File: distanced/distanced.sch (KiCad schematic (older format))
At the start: 20 parts

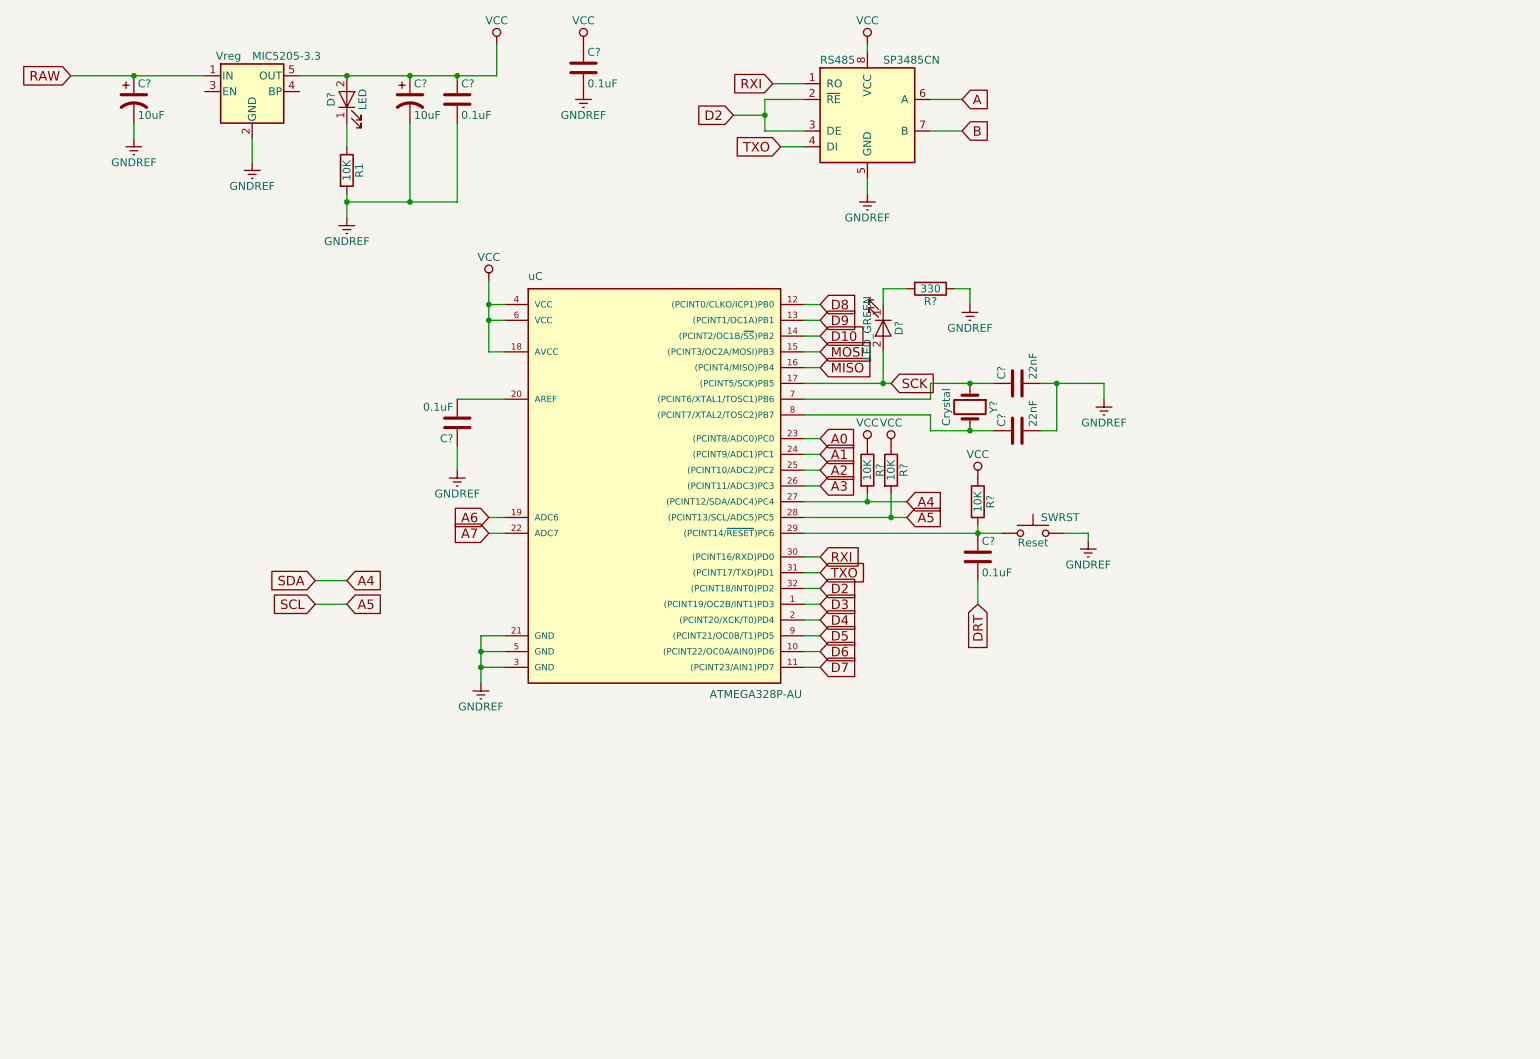
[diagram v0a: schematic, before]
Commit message: added the schematic of the ToF sensor
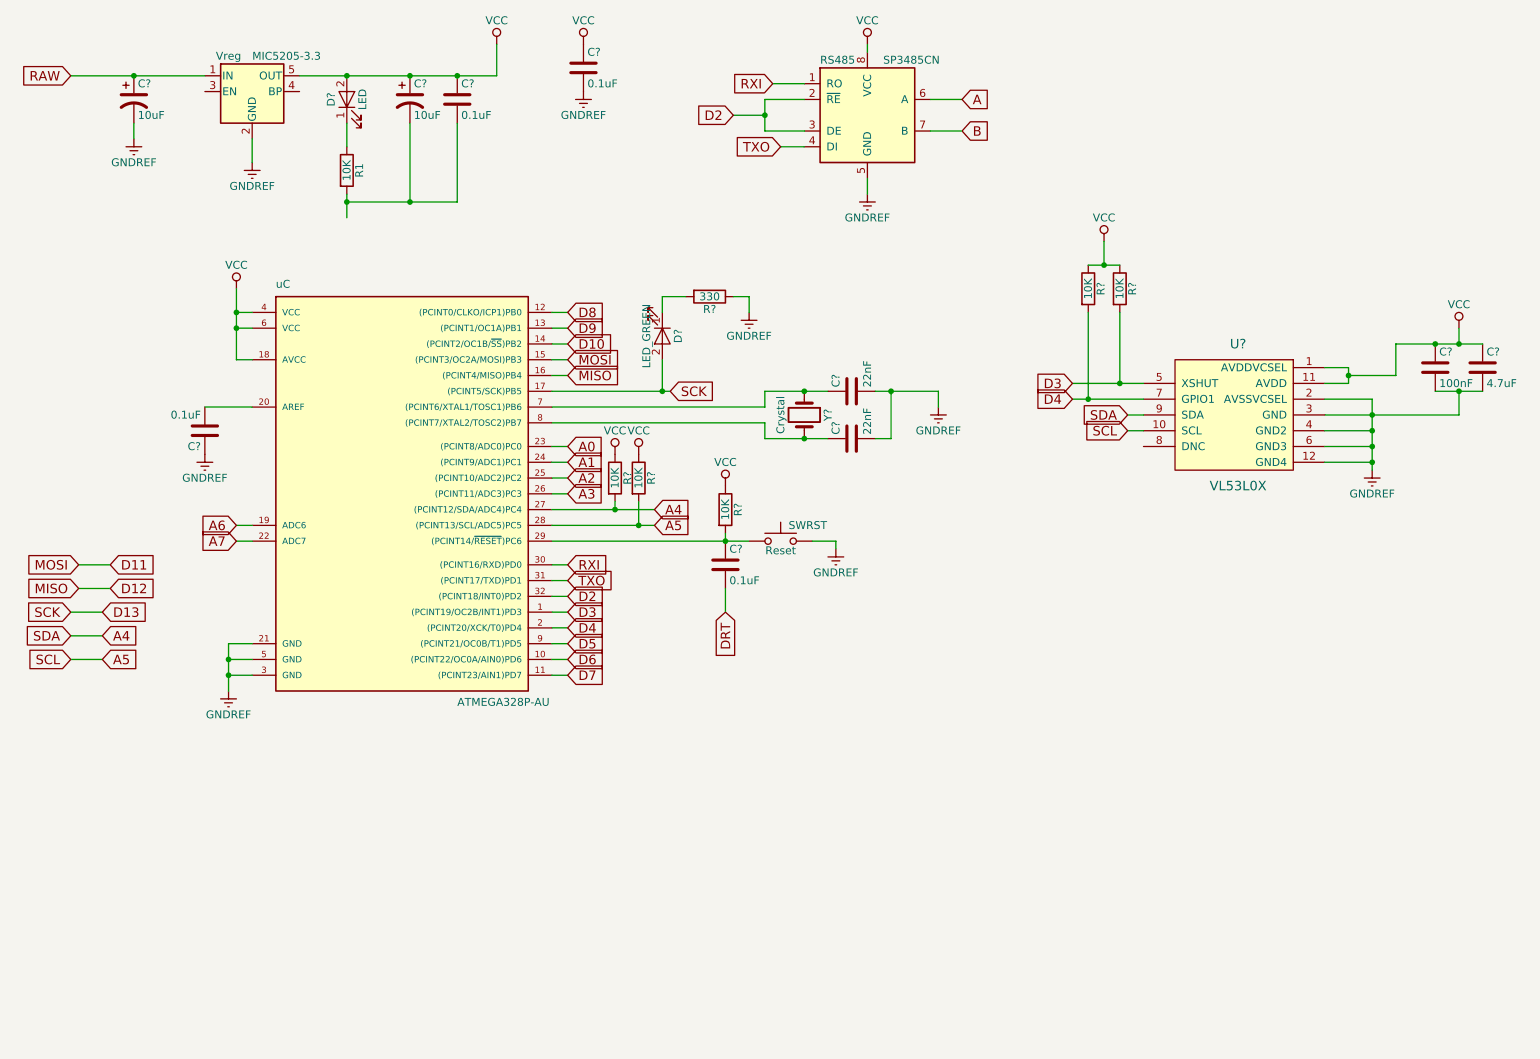
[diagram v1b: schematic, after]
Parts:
- added C?: 100nF, symbol C
- added C?: 4.7uF, symbol C
- added R? (x2): 10K, symbol R
- added U?: VL53L0X, symbol VL53L0X
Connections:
- net A4: now also U?.9 (SDA)
- net A5: now also U?.10 (SCL)
- net D3: now also R?.2, U?.5 (XSHUT)
- net D4: now also R?.2, U?.7 (GPIO1)
- net GNDREF: now also C?.2, C?.2, U?.12 (GND4), U?.2 (AVSSVCSEL), U?.3 (GND), U?.4 (GND2), U?.6 (GND3); no longer C?.2, C?.2, R1.2
- net VCC: now also C?.1, C?.1, R?.1, R?.1, U?.1 (AVDDVCSEL), U?.11 (AVDD)
- net MISO renamed D12
- net MOSI renamed D11
- net SCK renamed D13
- new net: C?.2, C?.2, R1.2
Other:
- moved on the sheet: C?, D?, R?, SWRST, Y?, uC

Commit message: added 2.8Vreg for tof and the ICSP FTDI and RS485 headers
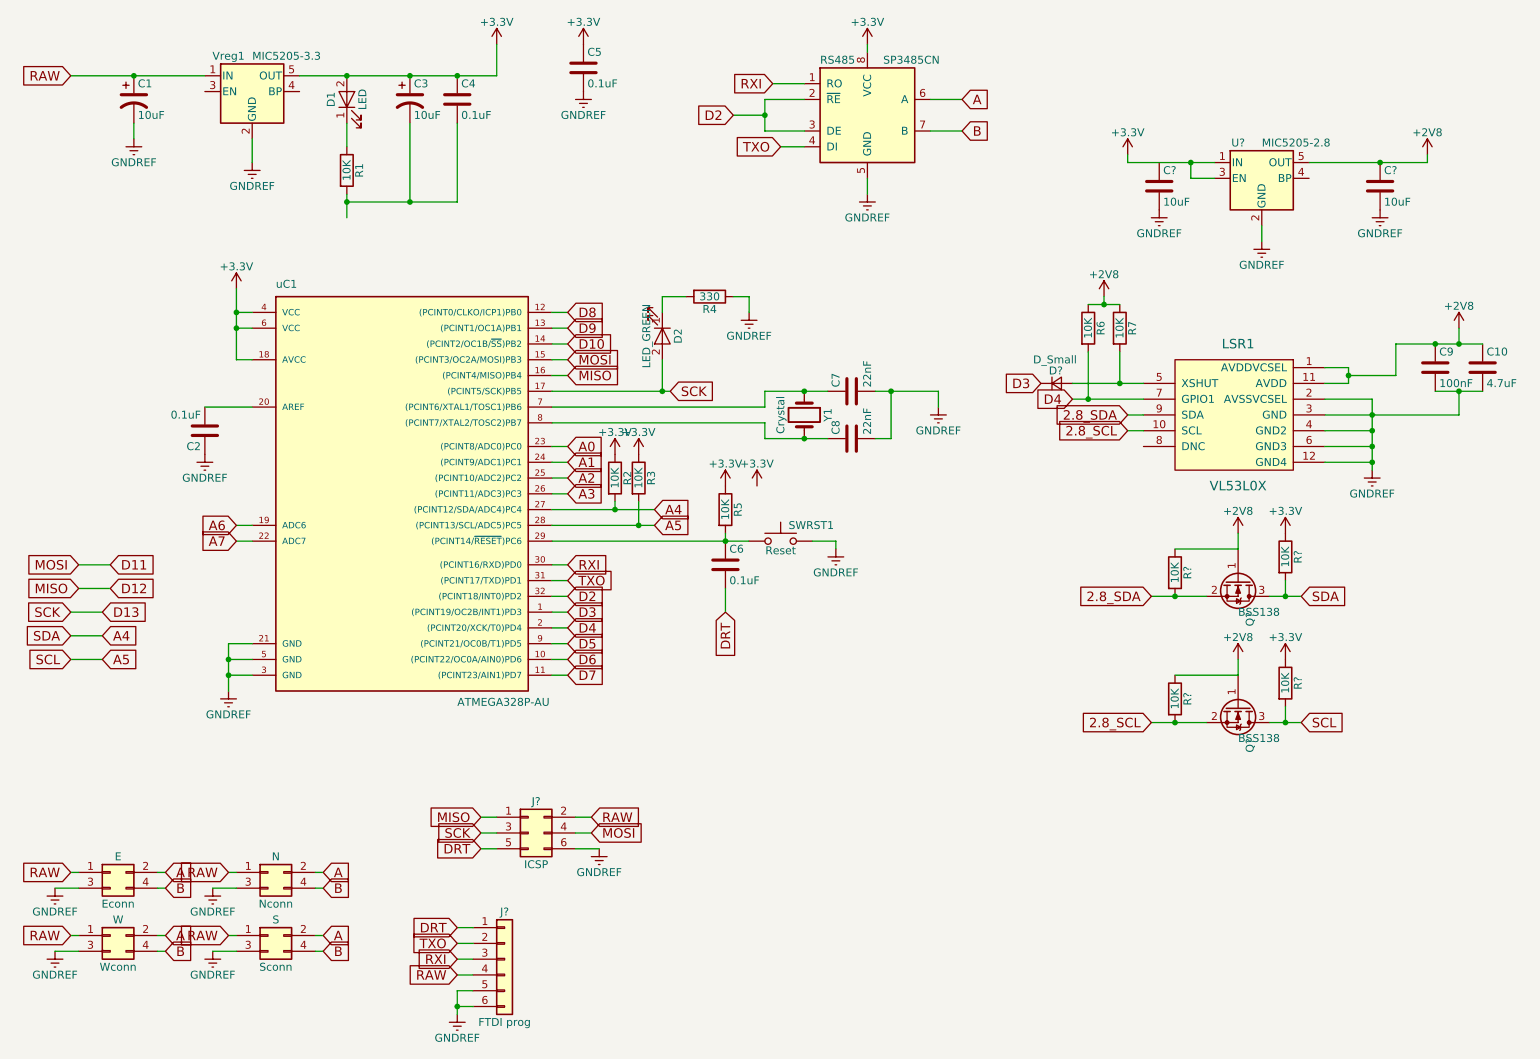
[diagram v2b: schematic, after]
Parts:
- added C? (x2): 10uF, Capacitors_SMD:C_0402, symbol C
- added D?: D_Small, symbol D_Small
- added E: Econn, symbol Conn_02x02_Odd_Even
- added J?: ICSP, symbol Conn_02x03_Odd_Even
- added J?: FTDI prog, symbol Conn_01x06
- added N: Nconn, symbol Conn_02x02_Odd_Even
- added Q? (x2): BSS138, TO_SOT_Packages_SMD:SOT-23, symbol BSS138
- added R? (x4): 10K, Resistors_SMD:R_0402, symbol R
- added S: Sconn, symbol Conn_02x02_Odd_Even
- added U?: MIC5205-2.8, TO_SOT_Packages_SMD:SOT-23-5, symbol MIC5205-2.8
- added W: Wconn, symbol Conn_02x02_Odd_Even
- C1, C3: renamed from C?; footprint (none) -> Capacitors_Tantalum_SMD:CP_Tantalum_Case-A_EIA-3216-18_Reflow
- C10, C2, C4, C5, C6, C7, C8, C9: renamed from C?; footprint (none) -> Capacitors_SMD:C_0402
- D1, D2: renamed from D?; footprint (none) -> LEDs:LED_0402
- LSR1: renamed from U?; footprint (none) -> VL53L0X:VL53L0X
- R1: footprint (none) -> Resistors_SMD:R_0402
- R2, R3, R4, R5, R6, R7: renamed from R?; footprint (none) -> Resistors_SMD:R_0402
- SWRST1: renamed from SWRST; footprint (none) -> Buttons_Switches_THT:SW_PUSH_6mm_h4.3mm
- Y1: renamed from Y?; footprint (none) -> Crystals:Crystal_SMD_2016-4pin_2.0x1.6mm
- renumbered Vreg to Vreg1, uC to uC1
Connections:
- net A: now also E.2 (Pin_2), N.2 (Pin_2), S.2 (Pin_2), W.2 (Pin_2)
- net A4: now also Q?.3 (D), R?.2; no longer LSR1.9 (SDA)
- net A5: now also Q?.3 (D), R?.2; no longer LSR1.10 (SCL)
- net B: now also E.4 (Pin_4), N.4 (Pin_4), S.4 (Pin_4), W.4 (Pin_4)
- net D11: now also J?.4 (Pin_4)
- net D12: now also J?.1 (Pin_1)
- net D13: now also J?.3 (Pin_3)
- net D3: now also D?.1 (K); no longer LSR1.5 (XSHUT), R7.2
- net DRT: now also J?.1 (Pin_1), J?.5 (Pin_5)
- net GNDREF: now also C?.2, C?.2, E.3 (Pin_3), J?.5 (Pin_5), J?.6 (Pin_6), J?.6 (Pin_6), N.3 (Pin_3), S.3 (Pin_3), U?.2 (GND), W.3 (Pin_3)
- net RAW: now also E.1 (Pin_1), J?.2 (Pin_2), J?.4 (Pin_4), N.1 (Pin_1), S.1 (Pin_1), W.1 (Pin_1)
- net RXI: now also J?.3 (Pin_3)
- net TXO: now also J?.2 (Pin_2)
- net VCC renamed +3V3
- net +3V3: now also R?.1, R?.1, U?.1 (IN), U?.3 (EN); no longer C10.1, C9.1, LSR1.1 (AVDDVCSEL), LSR1.11 (AVDD), R6.1, R7.1
- new net: D?.2 (A), LSR1.5 (XSHUT), R7.2
- new net +2V8: C10.1, C9.1, C?.1, LSR1.1 (AVDDVCSEL), LSR1.11 (AVDD), Q?.1 (G), Q?.1 (G), R6.1, R7.1, R?.1, R?.1, U?.5 (OUT)
- new net 2.8_SCL: LSR1.10 (SCL), Q?.2 (S), R?.2
- new net 2.8_SDA: LSR1.9 (SDA), Q?.2 (S), R?.2
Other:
- moved on the sheet: R6, R7
